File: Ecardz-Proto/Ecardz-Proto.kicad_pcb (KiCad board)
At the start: 2 copper layers, 110 x 90 mm, 68 parts, among them J1 Conn_02x06_Odd_Even, J2 Conn_01x24, J3 Conn_ARM_SWD_TagConnect_TC203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, J4 Conn_02x07_Odd_Even, J5 Conn_01x05, Q1 NMOS, U1 STM32L071K8Ux

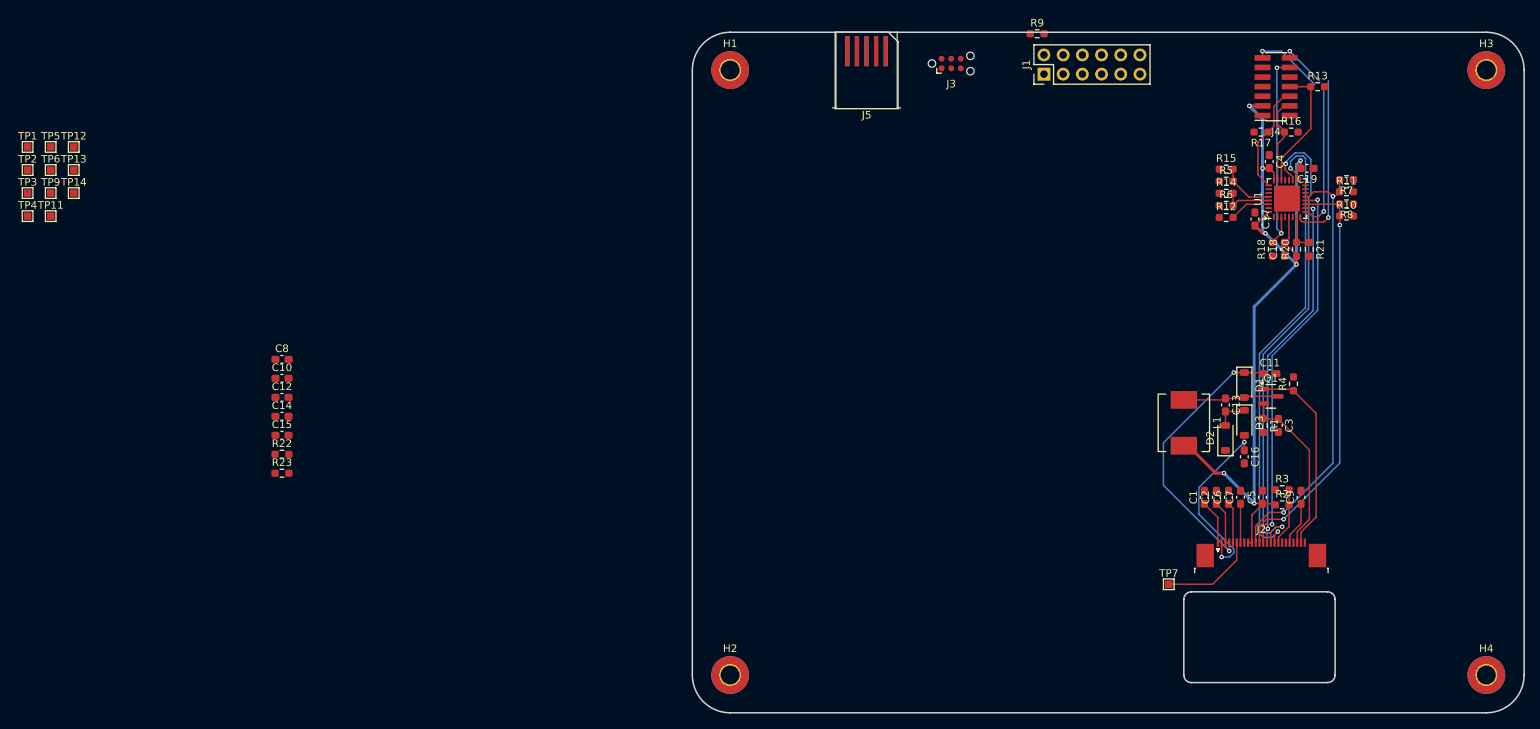
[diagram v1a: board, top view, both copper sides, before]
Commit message: rough layout complete
need to fix silkscreens and finish antenna
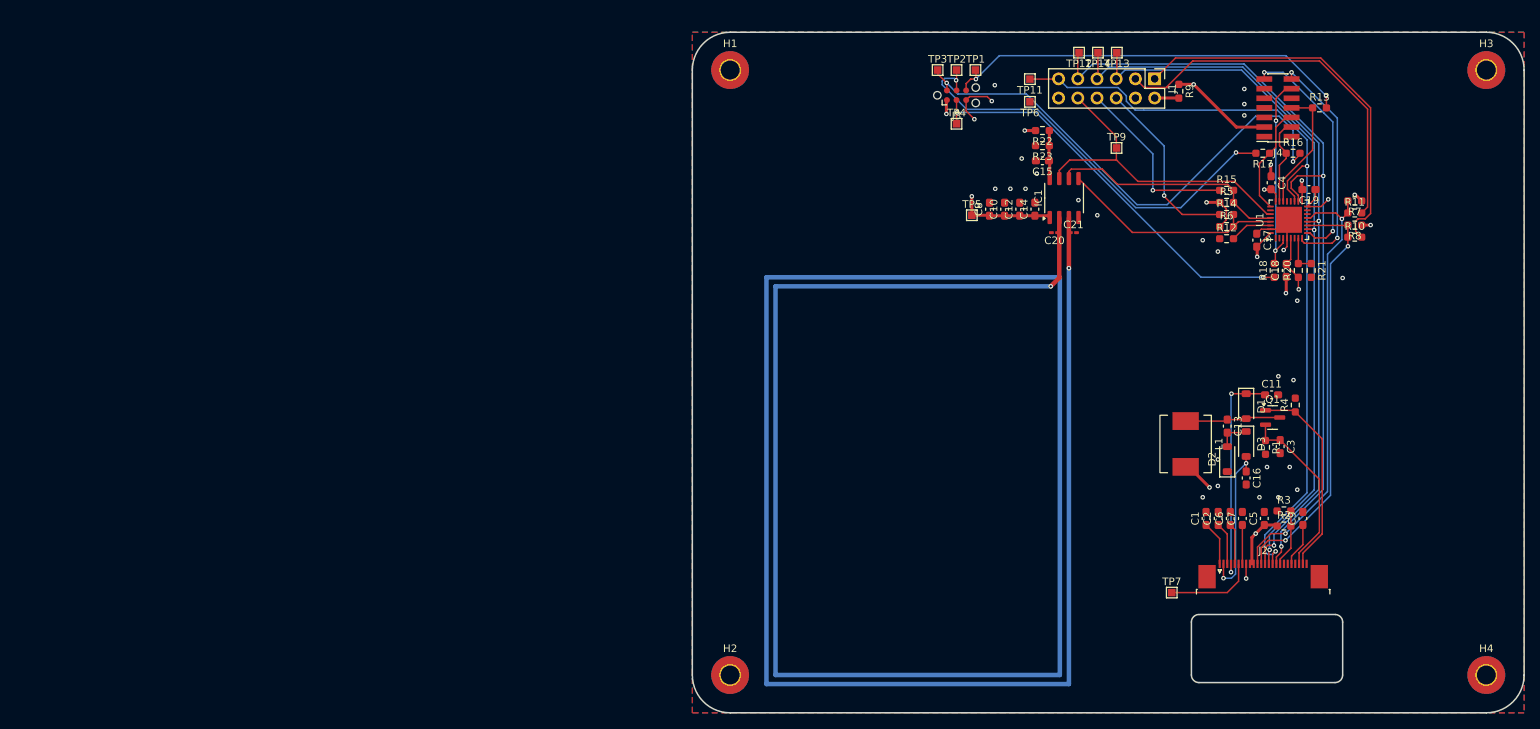
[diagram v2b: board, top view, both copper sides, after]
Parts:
- removed J5: Conn_01x05, Connector_PCBEdge:Samtec_MECF-05-0_-NP-L-DV_2x05_P1.27mm_Edge
- added C20: 7pF, Capacitor_SMD:C_0201_0603Metric_Pad0.64x0.40mm_HandSolder, F.Cu at (92.9, 71.5)
- added C21: 7pF, Capacitor_SMD:C_0201_0603Metric_Pad0.64x0.40mm_HandSolder, F.Cu at (95.4, 71.5)
- added IC1: M24LR04E-RMN6T/2, Package_SO:SO-8_3.9x4.9mm_P1.27mm, F.Cu at (94.2, 66.9)
- moved TP9 141.1 mm to (101.1, 60.3)
- moved TP13 138.8 mm to (101.1, 47.7), turned to 180 degrees
- moved TP14 136.7 mm to (98.6, 47.7), turned to 180 degrees
- moved TP12 133.5 mm to (96.1, 47.7), turned to 180 degrees
- moved TP11 130.8 mm to (89.6, 51.2), turned to 180 degrees
- moved TP6 129.8 mm to (89.6, 54.2), turned to 180 degrees
- moved TP1 125.8 mm to (82.4, 50.0)
- moved TP2 123.6 mm to (79.9, 50.0)
- moved TP4 123.5 mm to (79.9, 57.1)
- moved TP5 122.2 mm to (82.0, 69.2)
- moved TP3 121.4 mm to (77.4, 50.0)
- moved R23 109.5 mm to (91.3, 60.0), turned to 180 degrees
- moved R22 109.3 mm to (91.3, 58.0), turned to 180 degrees
- moved C15 106.9 mm to (91.3, 62.0), turned to 180 degrees
- moved C14 103.3 mm to (90.3, 68.4), turned to 90 degrees
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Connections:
- net Net-(IC1-VCC) renamed /NFC/VDD_NFC
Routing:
- net Net-(IC1-AC0): track 0.00 -> 383.9 mm, vias 0 -> 2
- net VDD: track 110.1 -> 211.2 mm, vias 7 -> 13
- net /STM/SWDIO_TAG: track 0.00 -> 66.9 mm, vias 0 -> 2
- net /STM/SWCLK_TAG: track 0.00 -> 56.7 mm, vias 0 -> 2
- net /STM/SWO_TAG: track 0.00 -> 55.1 mm, vias 0 -> 2
- net /STM/NRST_TAG: track 0.00 -> 54.2 mm, vias 0 -> 2
- net /STM/SPI_EINK_SCL_RPI: track 0.00 -> 51.2 mm
- net /STM/SPI_EINK_SDA_RPI: track 0.00 -> 49.4 mm
- net /EINK/CS#: track 50.5 -> 98.3 mm
- net /EINK/D/C#: track 47.7 -> 93.3 mm
- net /EINK/BUSY: track 62.0 -> 107.2 mm
- net /STM/NFC_BUSY: track 0.00 -> 43.7 mm
- net /EINK/RES#: track 64.9 -> 107.3 mm
- net GND: track 0.00 -> 27.6 mm, vias 0 -> 32
- net /STM/I2C_NFC_SCL: track 7.19 -> 31.5 mm
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- added copper zone on B.Cu, net GND
- added copper zone on F.Cu, net GND
- added copper zone on In1.Cu, net GND
- added copper zone on In2.Cu, net GND
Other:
- outline, holes or cut-outs redrawn
- copper layers 2 -> 4

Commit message: fit layout in 4.2in card size
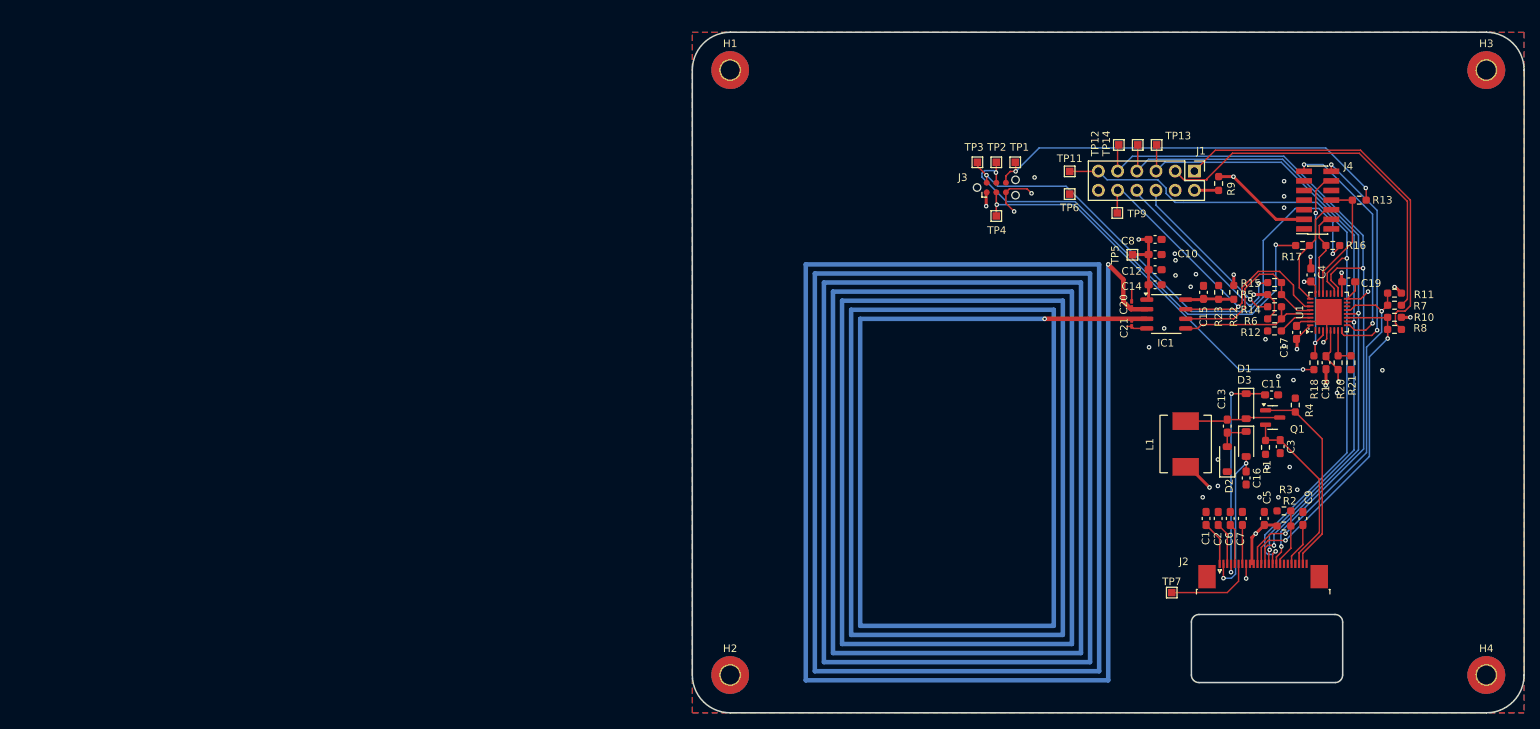
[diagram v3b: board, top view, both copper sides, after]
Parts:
- moved R22 33.1 mm to (116.6, 79.4), turned to 90 degrees
- moved R23 30.3 mm to (114.6, 79.4), turned to 90 degrees
- moved C15 27.5 mm to (112.6, 79.4), turned to 90 degrees
- moved C8 22.3 mm to (106.2, 72.4), turned to 0 degrees
- moved TP5 21.9 mm to (103.2, 74.4), turned to -90 degrees
- moved C10 20.8 mm to (106.2, 74.4), turned to 0 degrees
- moved IC1 20.4 mm to (107.7, 82.3), turned to 0 degrees
- moved C12 19.6 mm to (106.2, 76.4), turned to 0 degrees
- moved C14 18.8 mm to (106.2, 78.4), turned to 0 degrees
- moved C21 14.3 mm to (103.1, 83.5), turned to -90 degrees
- moved C20 13.9 mm to (103.1, 81.0), turned to 90 degrees
- moved R14 13.8 mm to (122.0, 81.3)
- moved R5 13.8 mm to (122.0, 79.7)
- moved R6 13.8 mm to (122.0, 82.9)
- moved R15 13.8 mm to (122.0, 78.1)
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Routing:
- net Net-(IC1-AC0): track 383.9 -> 1152.0 mm
- net VDD: track 211.2 -> 190.9 mm
- net /STM/I2C_NFC_SDA: track 30.6 -> 18.9 mm
- net /EINK/SDA: track 59.5 -> 49.5 mm
- net /EINK/SCL: track 56.3 -> 46.2 mm
- net /EINK/D/C#: track 93.3 -> 83.3 mm
- net /EINK/CS#: track 98.3 -> 88.3 mm
- net /EINK/RES#: track 107.3 -> 97.3 mm
- net /EINK/BUSY: track 107.2 -> 97.3 mm
- net /STM/I2C_NFC_SCL: track 31.5 -> 23.4 mm
- net /STM/SWDIO_TAG: track 66.9 -> 73.1 mm
- net /STM/SWCLK_TAG: track 56.7 -> 61.9 mm
- net /STM/NFC_BUSY: track 43.7 -> 48.6 mm, vias 0 -> 1
- net GND: track 27.6 -> 31.8 mm
- net /STM/I2C_NFC_SCL_RPI: track 24.1 -> 26.2 mm
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
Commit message: added more space around antenna
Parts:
- moved TP5 5.13 mm to (105.4, 69.8)
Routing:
- net /STM/I2C_NFC_SDA_RPI: track 22.3 -> 23.0 mm
- net VDD: track 190.9 -> 191.4 mm
- net GND: vias 32 -> 27

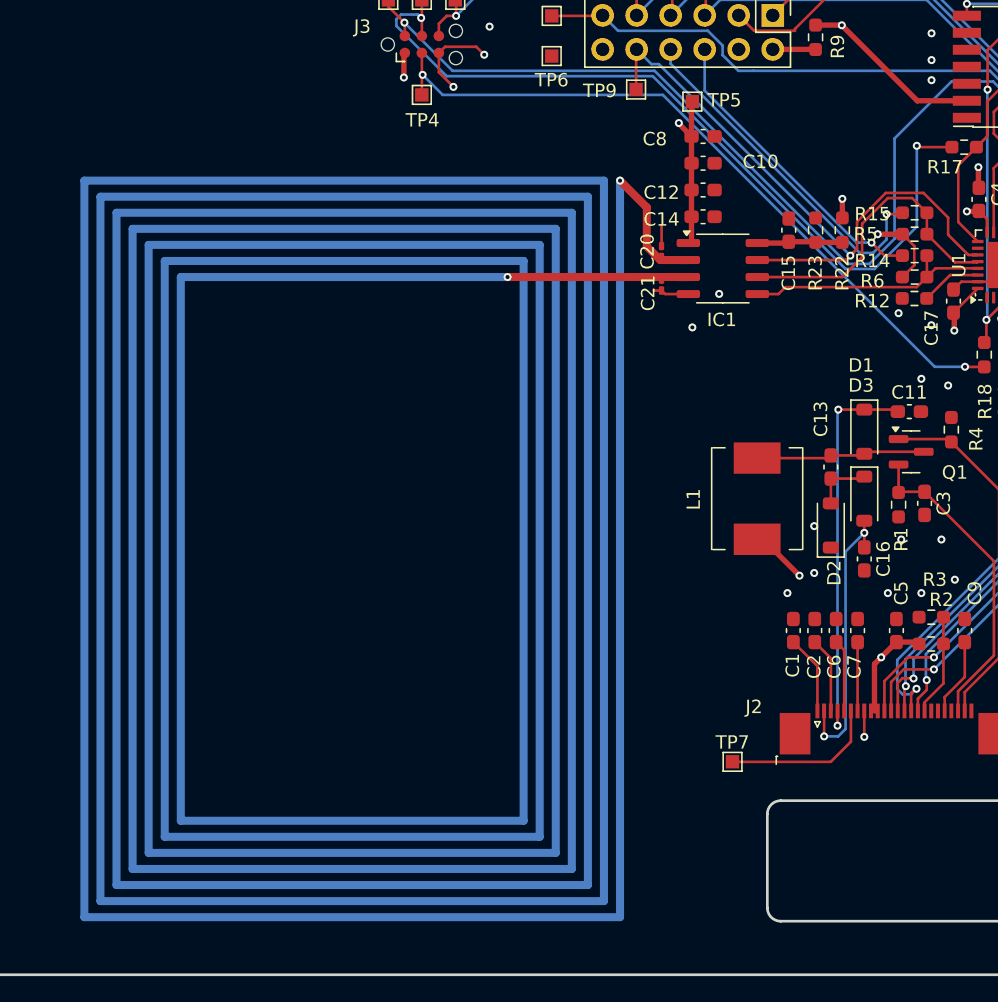
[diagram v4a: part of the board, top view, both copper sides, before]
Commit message: added large cap to layout
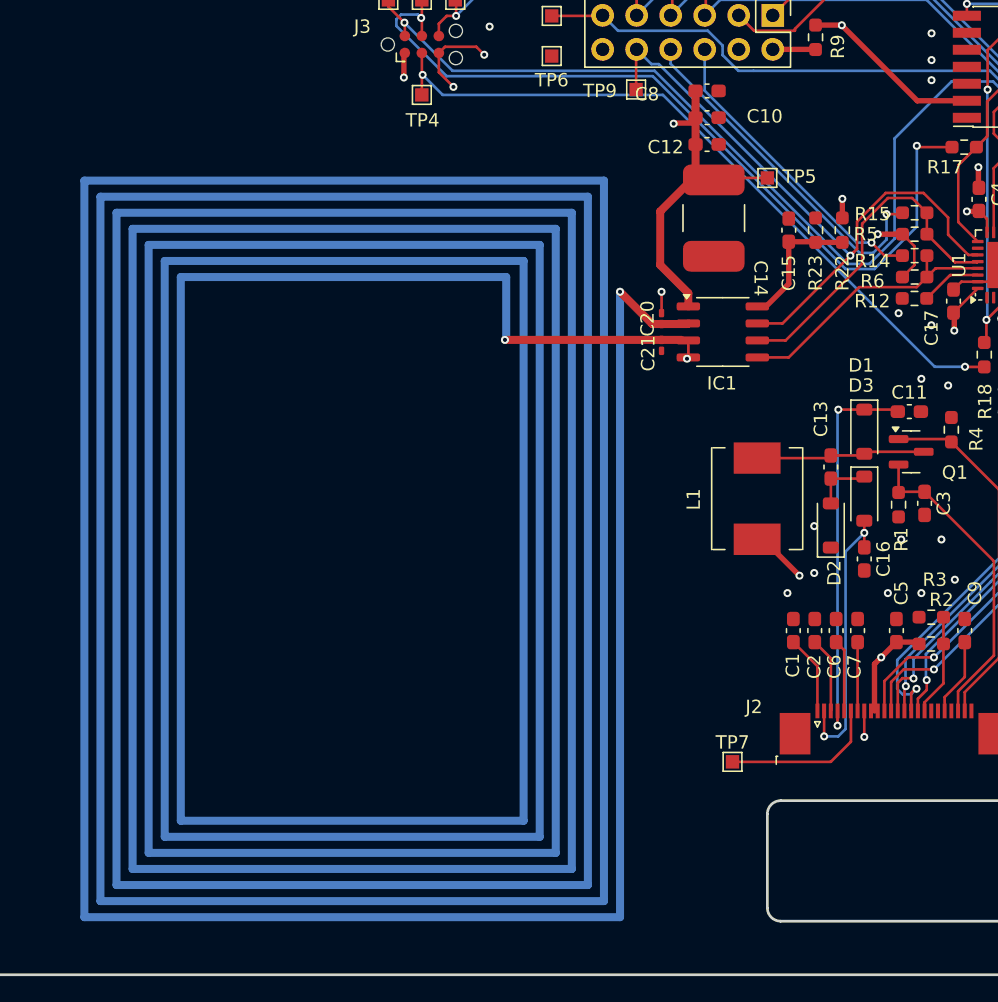
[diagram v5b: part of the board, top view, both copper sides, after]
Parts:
- C14: footprint Capacitor_SMD:C_0603_1608Metric_Pad1.08x0.95mm_HandSolder -> parts-lib:C_2917
- moved TP5 7.99 mm to (111.0, 75.5)
- moved C20 5.01 mm to (103.1, 86.0)
- moved IC1 4.73 mm to (107.7, 87.0)
- moved C21 4.50 mm to (103.1, 88.0)
- moved C10 3.41 mm to (106.5, 71.0)
- moved C12 3.41 mm to (106.5, 73.0)
- moved C8 3.41 mm to (106.5, 69.0)
- moved C14 0.81 mm to (107.0, 78.5), turned to -90 degrees
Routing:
- net VDD: track 191.4 -> 207.6 mm
- net Net-(IC1-AC0): track 1152.0 -> 1142.8 mm
- net /NFC/VDD_NFC: track 6.41 -> 10.2 mm
- net /STM/I2C_NFC_SCL: track 23.4 -> 25.6 mm
- net /STM/NFC_BUSY: track 48.6 -> 50.5 mm
- net /STM/I2C_NFC_SDA: track 18.9 -> 20.9 mm
- net GND: track 31.8 -> 30.4 mm

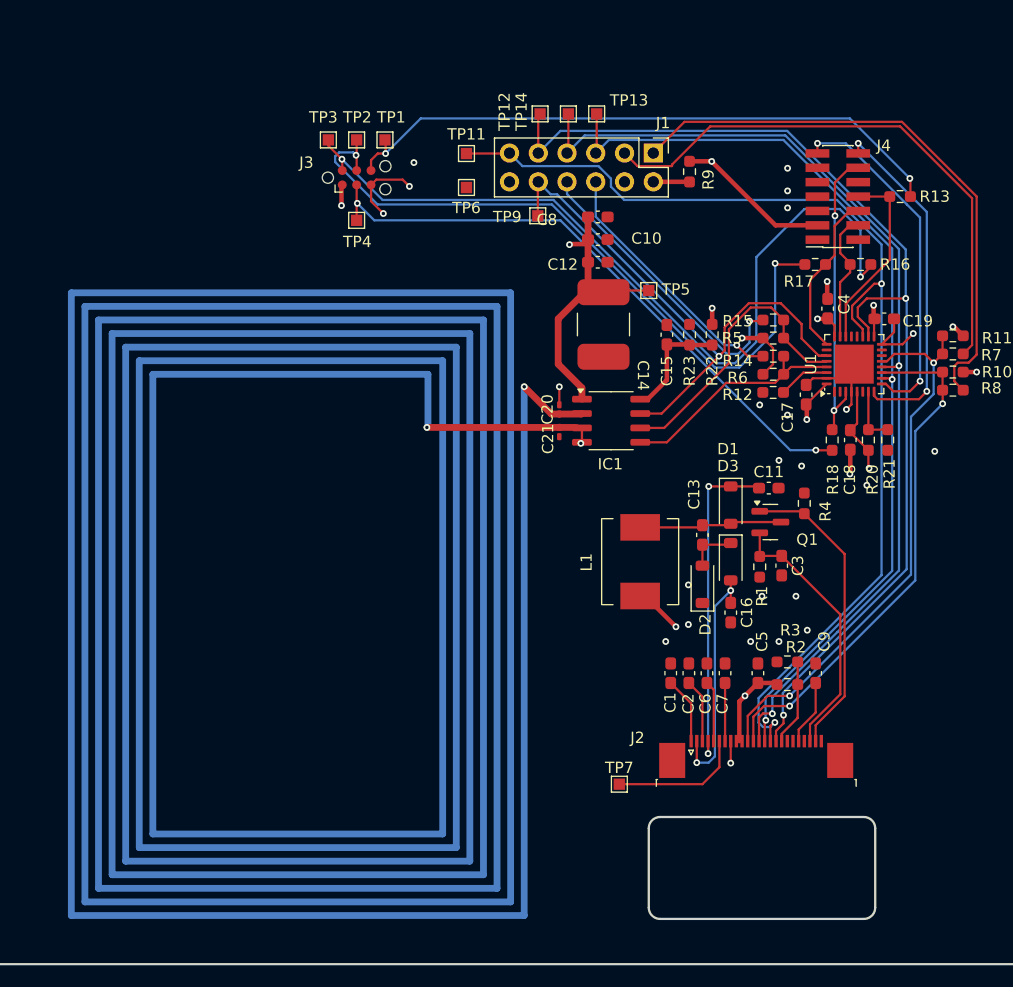
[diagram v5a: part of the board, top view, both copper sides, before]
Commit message: added zener and extra cap footprints
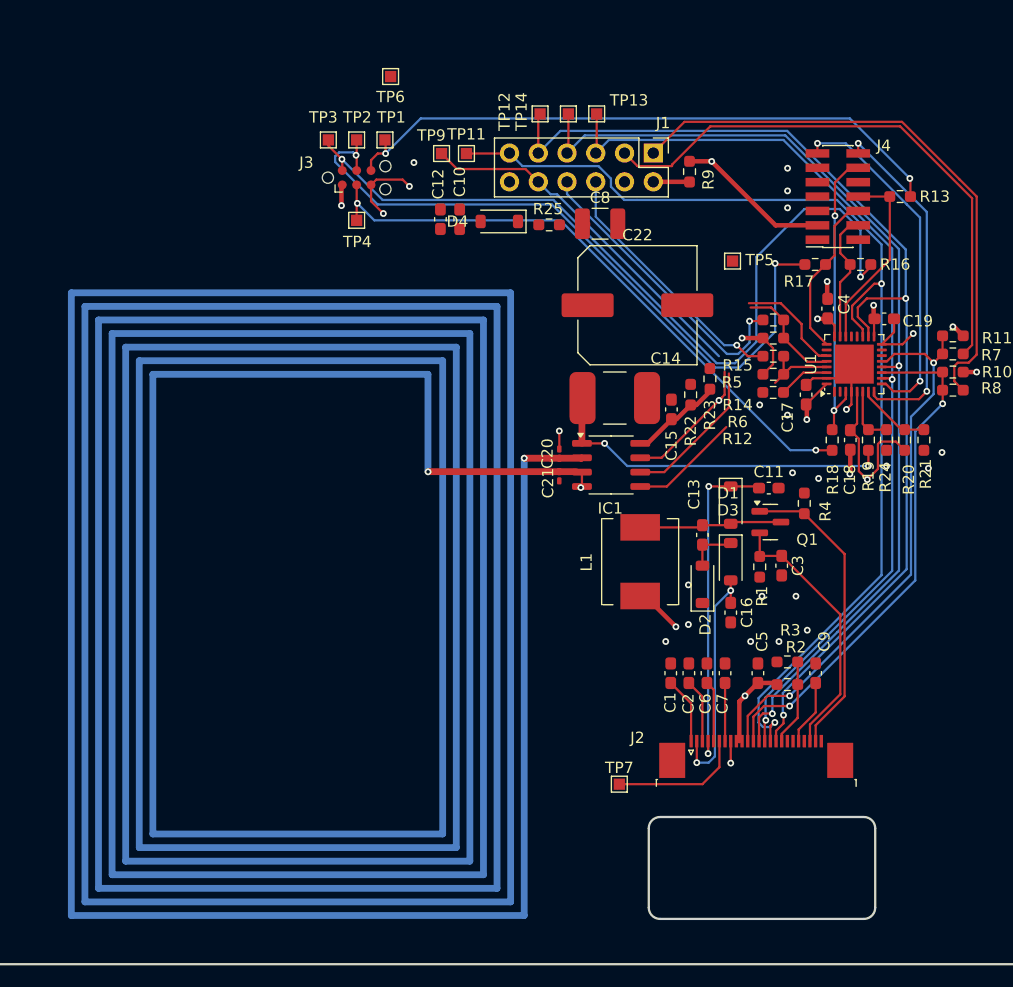
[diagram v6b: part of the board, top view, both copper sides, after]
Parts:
- added C22: TBD, Capacitor_SMD:C_Elec_10x10.2, F.Cu at (110.0, 76.8)
- added D4: D_Zener, Diode_SMD:D_SOD-123, F.Cu at (97.8, 69.4)
- added R19: 10k, Resistor_SMD:R_0603_1608Metric_Pad0.98x0.95mm_HandSolder, F.Cu at (130.4, 88.7)
- added R24: 10k, Resistor_SMD:R_0603_1608Metric_Pad0.98x0.95mm_HandSolder, F.Cu at (132.0, 88.7)
- added R25: 600R, Resistor_SMD:R_0603_1608Metric_Pad0.98x0.95mm_HandSolder, F.Cu at (102.2, 69.7)
- C8: footprint Capacitor_SMD:C_0603_1608Metric_Pad1.08x0.95mm_HandSolder -> Capacitor_SMD:C_1210_3225Metric_Pad1.33x2.70mm_HandSolder
- moved C12 14.4 mm to (92.6, 69.2), turned to -90 degrees
- moved C10 12.3 mm to (94.3, 69.2), turned to -90 degrees
- moved TP6 11.9 mm to (88.2, 56.6)
- moved TP9 10.1 mm to (92.7, 63.4)
- moved TP5 7.84 mm to (118.4, 72.9)
- moved C15 6.61 mm to (113.0, 86.0)
- moved C14 6.58 mm to (108.0, 85.0), turned to 0 degrees
- moved R22 5.63 mm to (114.7, 84.7)
- moved R23 4.30 mm to (116.4, 83.3)
- moved C20 3.91 mm to (103.1, 89.9)
- moved C21 3.91 mm to (103.1, 91.9)
- moved IC1 3.91 mm to (107.7, 90.9)
- moved R21 3.20 mm to (135.3, 88.7)
- moved R20 3.20 mm to (133.6, 88.7)
- moved C8 0.63 mm to (106.7, 69.6)
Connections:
- C14 pad 1: VDD -> /NFC/V_E_HARVEST
- C8 pad 1: VDD -> /NFC/V_E_HARVEST
- IC1 pad 1: VDD -> /NFC/V_E_HARVEST
- U1 pad 6: unconnected-(U1-PA0-Pad6) -> Net-(U1-PA0)
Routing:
- net /NFC/V_E_HARVEST: track 0.00 -> 31.8 mm, vias 0 -> 2
- net VDD: track 207.6 -> 181.9 mm, vias 13 -> 11
- net Net-(U1-PA0): track 0.00 -> 5.16 mm
- net /STM/I2C_NFC_SDA: track 20.9 -> 16.6 mm
- net Net-(IC1-AC0): track 1142.8 -> 1139.3 mm
- net /STM/NFC_BUSY: track 50.5 -> 54.1 mm
- net /STM/I2C_NFC_SCL: track 25.6 -> 22.9 mm
- net /NFC/VDD_NFC: track 10.2 -> 7.81 mm
- net /STM/VDD_MEAS: track 5.05 -> 6.54 mm
- net GND: vias 27 -> 28
